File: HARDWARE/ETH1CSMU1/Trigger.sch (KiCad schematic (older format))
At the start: 24 parts, among them U901 74AC125, U902 74AHC1G14, U903 NXE1S0305MC, U904 HCPL0710, U905 ACPL-214, U906 HCPL0710

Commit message: Commit
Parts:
- C901, C902, C904, C905: footprint (none) -> SMD:C_0603_Symbol1
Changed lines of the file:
@@
 F 0 "C901" H 1615 1296 50  0000 L CNN
 F 1 "100n" H 1615 1205 50  0000 L CNN
-F 2 "" H 1538 1100 50  0001 C CNN
+F 2 "SMD:C_0603_Symbol1" H 1538 1100 50  0001 C CNN
 F 3 "~" H 1500 1250 50  0001 C CNN
 	1    1500 1250
@@
 F 0 "C902" H 2115 1296 50  0000 L CNN
 F 1 "100n" H 2115 1205 50  0000 L CNN
-F 2 "" H 2038 1100 50  0001 C CNN
+F 2 "SMD:C_0603_Symbol1" H 2038 1100 50  0001 C CNN
 F 3 "~" H 2000 1250 50  0001 C CNN
 	1    2000 1250
@@
 F 0 "C904" H 2615 1296 50  0000 L CNN
 F 1 "100n" H 2615 1205 50  0000 L CNN
-F 2 "" H 2538 1100 50  0001 C CNN
+F 2 "SMD:C_0603_Symbol1" H 2538 1100 50  0001 C CNN
 F 3 "~" H 2500 1250 50  0001 C CNN
 	1    2500 1250
@@
 F 0 "C905" H 3115 1296 50  0000 L CNN
 F 1 "100n" H 3115 1205 50  0000 L CNN
-F 2 "" H 3038 1100 50  0001 C CNN
+F 2 "SMD:C_0603_Symbol1" H 3038 1100 50  0001 C CNN
 F 3 "~" H 3000 1250 50  0001 C CNN
 	1    3000 1250

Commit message: Footprints
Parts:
- R907, R908: footprint (none) -> SMD:R_0603_Symbol1
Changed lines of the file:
@@
 F 0 "R908" H 7470 5846 50  0000 L CNN
 F 1 "10k" H 7470 5755 50  0000 L CNN
-F 2 "" V 7330 5800 50  0001 C CNN
+F 2 "SMD:R_0603_Symbol1" V 7330 5800 50  0001 C CNN
 F 3 "~" H 7400 5800 50  0001 C CNN
 	1    7400 5800
@@
 F 0 "R907" H 5970 2596 50  0000 L CNN
 F 1 "10k" H 5970 2505 50  0000 L CNN
-F 2 "" V 5830 2550 50  0001 C CNN
+F 2 "SMD:R_0603_Symbol1" V 5830 2550 50  0001 C CNN
 F 3 "~" H 5900 2550 50  0001 C CNN
 	1    5900 2550

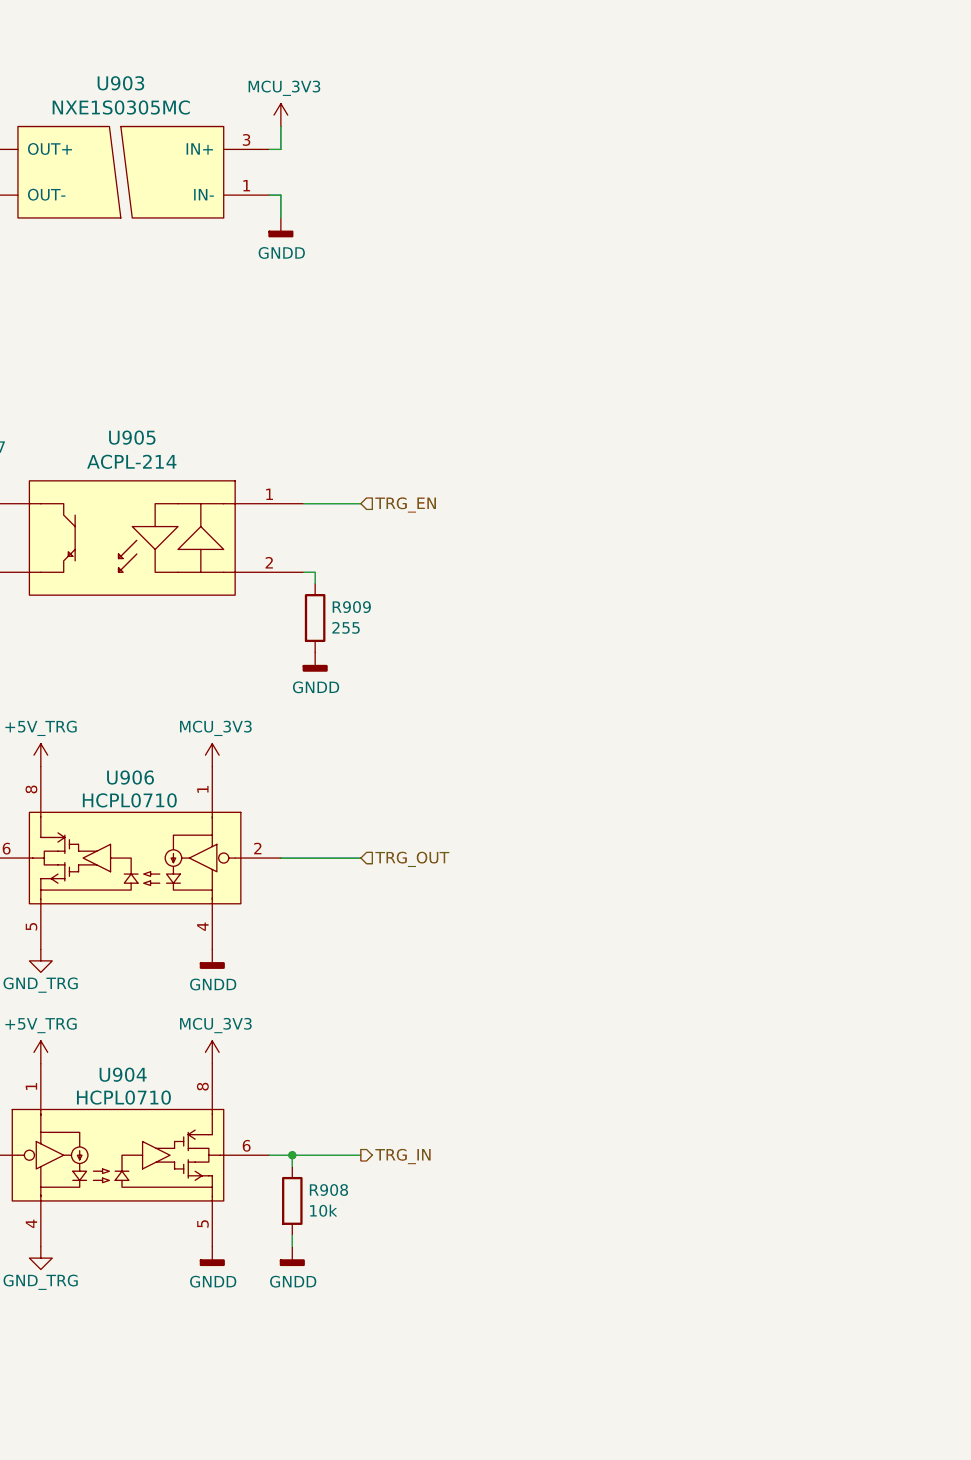
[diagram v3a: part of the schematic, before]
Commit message: Footprint selection
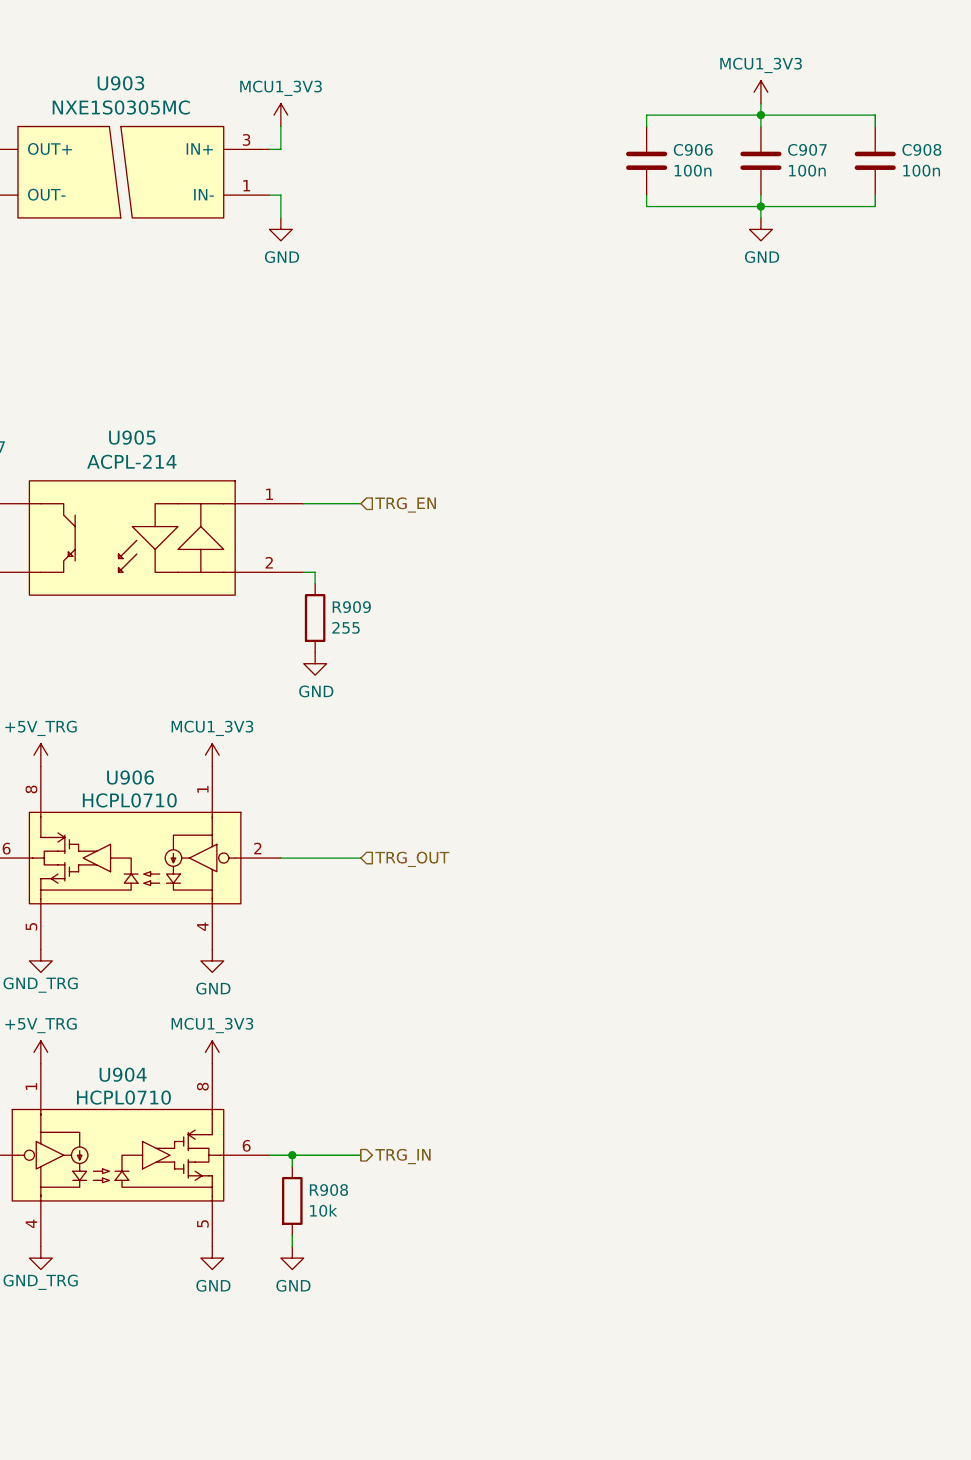
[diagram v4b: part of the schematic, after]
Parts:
- added C906, C907, C908: 100n, SMD:C_0603_Symbol1, symbol Device:C
- C903: footprint (none) -> Capacitors_SMD:C_0603
- R901, R902, R904, R906, R909: footprint (none) -> Resistors_SMD:R_0603
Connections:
- net GNDD is gone; now on net +5V_TRG: R908.2, R909.2, U903.1 (IN-), U904.5, U906.4
- net +5V_TRG: now also C906.2, C907.2, C908.2
- net MCU_3V3 renamed MCU1_3V3
- net MCU1_3V3: now also C906.1, C907.1, C908.1
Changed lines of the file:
@@
 F 0 "R901" H 2370 7046 50  0000 L CNN
 F 1 "51R1" H 2400 6950 50  0000 L CNN
-F 2 "" V 2230 7000 50  0001 C CNN
+F 2 "Resistors_SMD:R_0603" V 2230 7000 50  0001 C CNN
 F 3 "~" H 2300 7000 50  0001 C CNN
 	1    2300 7000
@@
 F 0 "C903" H 2415 6746 50  0000 L CNN
 F 1 "47p" H 2450 6650 50  0000 L CNN
-F 2 "" H 2338 6550 50  0001 C CNN
+F 2 "Capacitors_SMD:C_0603" H 2338 6550 50  0001 C CNN
 F 3 "~" H 2300 6700 50  0001 C CNN
 	1    2300 6700
@@
 F 0 "R902" V 2943 6500 50  0000 C CNN
 F 1 "47" V 3034 6500 50  0000 C CNN
-F 2 "" V 3080 6500 50  0001 C CNN
+F 2 "Resistors_SMD:R_0603" V 3080 6500 50  0001 C CNN
 F 3 "~" H 3150 6500 50  0001 C CNN
 	1    3150 6500
@@
 F 0 "R904" V 4043 6500 50  0000 C CNN
 F 1 "100" V 4134 6500 50  0000 C CNN
-F 2 "" V 4180 6500 50  0001 C CNN
+F 2 "Resistors_SMD:R_0603" V 4180 6500 50  0001 C CNN
 F 3 "~" H 4250 6500 50  0001 C CNN
 	1    4250 6500
@@
 $EndComp
 $Comp
-L power:GNDD #PWR0926
-U 1 1 5BA06C4E
-P 7050 6000
-F 0 "#PWR0926" H 7050 5750 50  0001 C CNN
-F 1 "GNDD" H 7054 5845 50  0000 C CNN
-F 2 "" H 7050 6000 50  0001 C CNN
-F 3 "" H 7050 6000 50  0001 C CNN
-	1    7050 6000
-	1    0    0    -1
-$EndComp
-$Comp
-L power_local:MCU_3V3 #PWR0925
-U 1 1 5BA0756C
-P 7050 5200
-F 0 "#PWR0925" H 7050 5050 50  0001 C CNN
-F 1 "MCU_3V3" H 7065 5373 50  0000 C CNN
-F 2 "" H 7050 5200 50  0000 C CNN
-F 3 "" H 7050 5200 50  0000 C CNN
-	1    7050 5200
-	1    0    0    -1
-$EndComp
-$Comp
 L Device:R R908
 U 1 1 5BA08A53
@@
 Wire Wire Line
 	7400 5600 7300 5600
-$Comp
-L power:GNDD #PWR0929
-U 1 1 5BA08CF1
-P 7400 6000
-F 0 "#PWR0929" H 7400 5750 50  0001 C CNN
-F 1 "GNDD" H 7404 5845 50  0000 C CNN
-F 2 "" H 7400 6000 50  0001 C CNN
-F 3 "" H 7400 6000 50  0001 C CNN
-	1    7400 6000
-	1    0    0    -1
-$EndComp
 Wire Wire Line
 	7400 6000 7400 5950
@@
 $EndComp
 $Comp
-L power_local:MCU_3V3 #PWR0923
-U 1 1 5BA0AE48
-P 7050 3900
-F 0 "#PWR0923" H 7050 3750 50  0001 C CNN
-F 1 "MCU_3V3" H 7065 4073 50  0000 C CNN
-F 2 "" H 7050 3900 50  0000 C CNN
-F 3 "" H 7050 3900 50  0000 C CNN
-	1    7050 3900
-	1    0    0    -1
-$EndComp
-$Comp
-L power:GNDD #PWR0924
-U 1 1 5BA0AE7D
-P 7050 4700
-F 0 "#PWR0924" H 7050 4450 50  0001 C CNN
-F 1 "GNDD" H 7054 4545 50  0000 C CNN
-F 2 "" H 7050 4700 50  0001 C CNN
-F 3 "" H 7050 4700 50  0001 C CNN
-	1    7050 4700
-	1    0    0    -1
-$EndComp
-$Comp
 L power_local:GND_TRG #PWR0920
 U 1 1 5BA0AF06
@@
 F 0 "R906" H 5520 4546 50  0000 L CNN
 F 1 "NC" H 5520 4455 50  0000 L CNN
-F 2 "" V 5380 4500 50  0001 C CNN
+F 2 "Resistors_SMD:R_0603" V 5380 4500 50  0001 C CNN
 F 3 "~" H 5450 4500 50  0001 C CNN
 	1    5450 4500
@@
 F 0 "R909" H 7570 3296 50  0000 L CNN
 F 1 "255" H 7570 3205 50  0000 L CNN
-F 2 "" V 7430 3250 50  0001 C CNN
+F 2 "Resistors_SMD:R_0603" V 7430 3250 50  0001 C CNN
 F 3 "~" H 7500 3250 50  0001 C CNN
 	1    7500 3250
@@
 Wire Wire Line
 	7500 3050 7450 3050
-$Comp
-L power:GNDD #PWR0930
-U 1 1 5BA1F766
-P 7500 3400
-F 0 "#PWR0930" H 7500 3150 50  0001 C CNN
-F 1 "GNDD" H 7504 3245 50  0000 C CNN
-F 2 "" H 7500 3400 50  0001 C CNN
-F 3 "" H 7500 3400 50  0001 C CNN
-	1    7500 3400
-	1    0    0    -1
-$EndComp
 $Comp
 L Device:R R907
@@
 	-1   0    0    -1
 $EndComp
-$Comp
-L power_local:MCU_3V3 #PWR0927
-U 1 1 5BBFBA45
-P 7350 1100
-F 0 "#PWR0927" H 7350 950 50  0001 C CNN
-F 1 "MCU_3V3" H 7365 1273 50  0000 C CNN
-F 2 "" H 7350 1100 50  0000 C CNN
-F 3 "" H 7350 1100 50  0000 C CNN
-	1    7350 1100
-	1    0    0    -1
-$EndComp
 Wire Wire Line
 	7350 1100 7350 1200
 Wire Wire Line
 	7350 1200 7300 1200
-$Comp
-L power:GNDD #PWR0928
-U 1 1 5BBFD8C3
-P 7350 1500
-F 0 "#PWR0928" H 7350 1250 50  0001 C CNN
-F 1 "GNDD" H 7354 1345 50  0000 C CNN
-F 2 "" H 7350 1500 50  0001 C CNN
-F 3 "" H 7350 1500 50  0001 C CNN
-	1    7350 1500
-	1    0    0    -1
-$EndComp
 Wire Wire Line
 	7350 1500 7350 1400
@@
 Wire Wire Line
 	2250 1050 2500 1050
+$Comp
+L Device:C C906
+U 1 1 5C0374B2
+P 8950 1250
+F 0 "C906" H 9065 1296 50  0000 L CNN
+F 1 "100n" H 9065 1205 50  0000 L CNN
+F 2 "SMD:C_0603_Symbol1" H 8988 1100 50  0001 C CNN
+F 3 "~" H 8950 1250 50  0001 C CNN
+	1    8950 1250
+	1    0    0    -1
+$EndComp
+$Comp
+L Device:C C907
+U 1 1 5C039594
+P 9450 1250
+F 0 "C907" H 9565 1296 50  0000 L CNN
+F 1 "100n" H 9565 1205 50  0000 L CNN
+F 2 "SMD:C_0603_Symbol1" H 9488 1100 50  0001 C CNN
+F 3 "~" H 9450 1250 50  0001 C CNN
+	1    9450 1250
+	1    0    0    -1
+$EndComp
+$Comp
+L Device:C C908
+U 1 1 5C039604
+P 9950 1250
+F 0 "C908" H 10065 1296 50  0000 L CNN
+F 1 "100n" H 10065 1205 50  0000 L CNN
+F 2 "SMD:C_0603_Symbol1" H 9988 1100 50  0001 C CNN
+F 3 "~" H 9950 1250 50  0001 C CNN
+	1    9950 1250
+	1    0    0    -1
+$EndComp
+Wire Wire Line
+	8950 1400 8950 1450
+Wire Wire Line
+	8950 1450 9450 1450
+Wire Wire Line
+	9950 1450 9950 1400
+Wire Wire Line
+	9450 1400 9450 1450
+Connection ~ 9450 1450
+Wire Wire Line
+	9450 1450 9950 1450
+Wire Wire Line
+	8950 1100 8950 1050
+Wire Wire Line
+	8950 1050 9450 1050
+Wire Wire Line
+	9950 1050 9950 1100
+Wire Wire Line
+	9450 1100 9450 1050
+Connection ~ 9450 1050
+Wire Wire Line
+	9450 1050 9950 1050
+$Comp
+L power_local:MCU1_3V3 #PWR0927
+U 1 1 5C048613
+P 7350 1100
+F 0 "#PWR0927" H 7350 1000 50  0001 C CNN
+F 1 "MCU1_3V3" H 7350 1273 50  0000 C CNN
+F 2 "" H 7350 1100 50  0000 C CNN
+F 3 "" H 7350 1100 50  0000 C CNN
+	1    7350 1100
+	1    0    0    -1
+$EndComp
+$Comp
+L power_local:MCU1_3V3 #PWR0923
+U 1 1 5C048AAD
+P 7050 3900
+F 0 "#PWR0923" H 7050 3800 50  0001 C CNN
+F 1 "MCU1_3V3" H 7050 4073 50  0000 C CNN
+F 2 "" H 7050 3900 50  0000 C CNN
+F 3 "" H 7050 3900 50  0000 C CNN
+	1    7050 3900
+	1    0    0    -1
+$EndComp
+$Comp
+L power_local:MCU1_3V3 #PWR0925
+U 1 1 5C048D05
+P 7050 5200
+F 0 "#PWR0925" H 7050 5100 50  0001 C CNN
+F 1 "MCU1_3V3" H 7050 5373 50  0000 C CNN
+F 2 "" H 7050 5200 50  0000 C CNN
+F 3 "" H 7050 5200 50  0000 C CNN
+	1    7050 5200
+	1    0    0    -1
+$EndComp
+$Comp
+L power_local:MCU1_3V3 #PWR0931
+U 1 1 5C048E46
+P 9450 1000
+F 0 "#PWR0931" H 9450 900 50  0001 C CNN
+F 1 "MCU1_3V3" H 9450 1173 50  0000 C CNN
+F 2 "" H 9450 1000 50  0000 C CNN
+F 3 "" H 9450 1000 50  0000 C CNN
+	1    9450 1000
+	1    0    0    -1
+$EndComp
+Wire Wire Line
+	9450 1000 9450 1050
+$Comp
+L power:GND #PWR0926
+U 1 1 5C04C0FF
+P 7050 6000
+F 0 "#PWR0926" H 7050 5750 50  0001 C CNN
+F 1 "GND" H 7055 5827 50  0000 C CNN
+F 2 "" H 7050 6000 50  0001 C CNN
+F 3 "" H 7050 6000 50  0001 C CNN
+	1    7050 6000
+	1    0    0    -1
+$EndComp
+$Comp
+L power:GND #PWR0929
+U 1 1 5C04C14F
+P 7400 6000
+F 0 "#PWR0929" H 7400 5750 50  0001 C CNN
+F 1 "GND" H 7405 5827 50  0000 C CNN
+F 2 "" H 7400 6000 50  0001 C CNN
+F 3 "" H 7400 6000 50  0001 C CNN
+	1    7400 6000
+	1    0    0    -1
+$EndComp
+$Comp
+L power:GND #PWR0924
+U 1 1 5C04C198
+P 7050 4700
+F 0 "#PWR0924" H 7050 4450 50  0001 C CNN
+F 1 "GND" H 7055 4527 50  0000 C CNN
+F 2 "" H 7050 4700 50  0001 C CNN
+F 3 "" H 7050 4700 50  0001 C CNN
+	1    7050 4700
+	1    0    0    -1
+$EndComp
+$Comp
+L power:GND #PWR0930
+U 1 1 5C04C336
+P 7500 3400
+F 0 "#PWR0930" H 7500 3150 50  0001 C CNN
+F 1 "GND" H 7505 3227 50  0000 C CNN
+F 2 "" H 7500 3400 50  0001 C CNN
+F 3 "" H 7500 3400 50  0001 C CNN
+	1    7500 3400
+	1    0    0    -1
+$EndComp
+$Comp
+L power:GND #PWR0928
+U 1 1 5C04C477
+P 7350 1500
+F 0 "#PWR0928" H 7350 1250 50  0001 C CNN
+F 1 "GND" H 7355 1327 50  0000 C CNN
+F 2 "" H 7350 1500 50  0001 C CNN
+F 3 "" H 7350 1500 50  0001 C CNN
+	1    7350 1500
+	1    0    0    -1
+$EndComp
+$Comp
+L power:GND #PWR0932
+U 1 1 5C04C5D7
+P 9450 1500
+F 0 "#PWR0932" H 9450 1250 50  0001 C CNN
+F 1 "GND" H 9455 1327 50  0000 C CNN
+F 2 "" H 9450 1500 50  0001 C CNN
+F 3 "" H 9450 1500 50  0001 C CNN
+	1    9450 1500
+	1    0    0    -1
+$EndComp
+Wire Wire Line
+	9450 1500 9450 1450
 $EndSCHEMATC

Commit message: Redesigned feedback circuit.
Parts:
- D902: footprint (none) -> SMD:DO_214AA_REV
- D903: footprint (none) -> SMD:SOT23
- R905: footprint (none) -> Resistors_SMD:R_0603
- U901: footprint (none) -> Housings_SOIC:SOIC-14_3.9x8.7mm_Pitch1.27mm
- U902: footprint (none) -> SMD:SC-70-5
- U903: footprint (none) -> SMD:NXE1
- U904, U906: footprint (none) -> SMD:SOIC8NB
- U905: footprint (none) -> SMD:SO4
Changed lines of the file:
@@
 F 0 "D903" V 3500 6650 50  0000 L CNN
 F 1 "BAV99" V 3400 6650 50  0000 L CNN
-F 2 "" H 3600 6500 50  0001 C CNN
+F 2 "SMD:SOT23" H 3600 6500 50  0001 C CNN
 F 3 "" H 3600 6500 50  0000 C CNN
 	1    3600 6500
@@
 F 0 "D902" V 3004 5879 50  0000 L CNN
 F 1 "SMBJ5.0A" V 3095 5879 50  0000 L CNN
-F 2 "" H 3050 5800 50  0001 C CNN
+F 2 "SMD:DO_214AA_REV" H 3050 5800 50  0001 C CNN
 F 3 "~" H 3050 5800 50  0001 C CNN
 	1    3050 5800
@@
 F 0 "R905" V 4743 6500 50  0000 C CNN
 F 1 "14k7" V 4834 6500 50  0000 C CNN
-F 2 "" V 4880 6500 50  0001 C CNN
+F 2 "Resistors_SMD:R_0603" V 4880 6500 50  0001 C CNN
 F 3 "~" H 4950 6500 50  0001 C CNN
 	1    4950 6500
@@
 F 0 "U904" H 6550 5950 60  0000 L CNN
 F 1 "HCPL0710" H 6450 5850 60  0000 L CNN
-F 2 "" H 6225 5600 60  0001 C CNN
+F 2 "SMD:SOIC8NB" H 6225 5600 60  0001 C CNN
 F 3 "" H 6225 5600 60  0001 C CNN
 	1    6650 5600
@@
 F 0 "U906" H 6600 4650 60  0000 L CNN
 F 1 "HCPL0710" H 6500 4550 60  0000 L CNN
-F 2 "" H 6275 4300 60  0001 C CNN
+F 2 "SMD:SOIC8NB" H 6275 4300 60  0001 C CNN
 F 3 "" H 6275 4300 60  0001 C CNN
 	1    6700 4300
@@
 F 0 "U901" H 3750 4750 50  0000 C CNN
 F 1 "74AC125" H 3750 4500 40  0000 C CNN
-F 2 "" H 3550 4600 60  0001 C CNN
+F 2 "Housings_SOIC:SOIC-14_3.9x8.7mm_Pitch1.27mm" H 3550 4600 60  0001 C CNN
 F 3 "" H 3550 4600 60  0000 C CNN
 	4    3550 4600
@@
 F 0 "U901" H 3750 4000 50  0000 C CNN
 F 1 "74AC125" H 3750 3750 40  0000 C CNN
-F 2 "" H 3550 3850 60  0001 C CNN
+F 2 "Housings_SOIC:SOIC-14_3.9x8.7mm_Pitch1.27mm" H 3550 3850 60  0001 C CNN
 F 3 "" H 3550 3850 60  0000 C CNN
 	3    3550 3850
@@
 F 0 "U901" H 3750 3250 50  0000 C CNN
 F 1 "74AC125" H 3750 3000 40  0000 C CNN
-F 2 "" H 3550 3100 60  0001 C CNN
+F 2 "Housings_SOIC:SOIC-14_3.9x8.7mm_Pitch1.27mm" H 3550 3100 60  0001 C CNN
 F 3 "" H 3550 3100 60  0000 C CNN
 	2    3550 3100
@@
 F 0 "U905" H 6700 3337 60  0000 C CNN
 F 1 "ACPL-214" H 6700 3231 60  0000 C CNN
-F 2 "" H 6800 2850 60  0001 C CNN
+F 2 "SMD:SO4" H 6800 2850 60  0001 C CNN
 F 3 "" H 6800 2850 60  0000 C CNN
 	1    6700 2900
@@
 F 0 "U901" H 5150 5850 50  0000 C CNN
 F 1 "74AC125" H 5150 5750 50  0000 C CNN
-F 2 "" H 4950 5600 60  0001 C CNN
+F 2 "Housings_SOIC:SOIC-14_3.9x8.7mm_Pitch1.27mm" H 4950 5600 60  0001 C CNN
 F 3 "" H 4950 5600 60  0000 C CNN
 	1    4950 5600
@@
 F 0 "U902" H 5700 2550 50  0000 C CNN
 F 1 "74AHC1G14" H 5700 2650 50  0000 C CNN
-F 2 "" H 5450 2750 50  0001 C CNN
+F 2 "SMD:SC-70-5" H 5450 2750 50  0001 C CNN
 F 3 "http://www.ti.com/lit/sg/scyt129e/scyt129e.pdf" H 5450 2750 50  0001 C CNN
 	1    5450 2750
@@
 F 0 "U901" H 1050 1350 50  0000 C CNN
 F 1 "74AC125" H 1050 1250 50  0000 C CNN
-F 2 "" H 750 1300 60  0001 C CNN
+F 2 "Housings_SOIC:SOIC-14_3.9x8.7mm_Pitch1.27mm" H 750 1300 60  0001 C CNN
 F 3 "" H 750 1300 60  0000 C CNN
 	5    750  1300
@@
 F 0 "U903" H 6650 1687 60  0000 C CNN
 F 1 "NXE1S0305MC" H 6650 1581 60  0000 C CNN
-F 2 "" H 6650 1300 60  0001 C CNN
+F 2 "SMD:NXE1" H 6650 1300 60  0001 C CNN
 F 3 "" H 6650 1300 60  0001 C CNN
 	1    6650 1300

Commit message: Schematic development
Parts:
- renumbered C901 to C801, C902 to C802, C903 to C803, C904 to C804, C905 to C805, C906 to C806, C907 to C807, C908 to C808, D901 to D801, D902 to D802, D903 to D803, L901 to L801, R901 to R801, R902 to R802, R903 to R803, R904 to R804, R905 to R805, R906 to R806, R907 to R807, R908 to R808, R909 to R809, U901 to U801, U902 to U802, U903 to U803, U904 to U804, U905 to U805, U906 to U806

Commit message: check in
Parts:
- D801: footprint (none) -> Diodes_SMD:D_SOD-323_HandSoldering
- L801: footprint (none) -> SMD:CW252016
- R803: footprint (none) -> SMD:R_0603_Symbol9
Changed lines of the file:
@@
 F 0 "D801" V 1500 7050 50  0000 L CNN
 F 1 "SD36C-01FTG" V 1595 6929 50  0000 L CNN
-F 2 "" H 1550 6850 50  0001 C CNN
+F 2 "Diodes_SMD:D_SOD-323_HandSoldering" H 1550 6850 50  0001 C CNN
 F 3 "~" H 1550 6850 50  0001 C CNN
 	1    1550 6850
@@
 F 0 "L801" V 2790 6500 50  0000 C CNN
 F 1 "CW252016-R33G" V 2699 6500 50  0000 C CNN
-F 2 "" H 2600 6500 50  0001 C CNN
+F 2 "SMD:CW252016" H 2600 6500 50  0001 C CNN
 F 3 "~" H 2600 6500 50  0001 C CNN
 	1    2600 6500
@@
 F 0 "R803" H 3670 5446 50  0000 L CNN
 F 1 "1k" H 3670 5355 50  0000 L CNN
-F 2 "" V 3530 5400 50  0001 C CNN
+F 2 "SMD:R_0603_Symbol9" V 3530 5400 50  0001 C CNN
 F 3 "~" H 3600 5400 50  0001 C CNN
 	1    3600 5400
